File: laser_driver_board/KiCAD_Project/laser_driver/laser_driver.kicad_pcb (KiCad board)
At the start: 2 copper layers, 76.2 x 33 mm, 10 parts, among them J1 Input, J2 Output, U1 MLD203CLNE

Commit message: Finalize laser driver board.
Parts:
- moved TP2 27.0 mm to (161.8, 105.4)
- moved TP1 17.9 mm to (154.2, 105.4)
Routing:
- net /ISENS-: track 6.46 -> 27.3 mm
- net /ISENS+: track 7.51 -> 18.5 mm
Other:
- board text added: "LG 3-0000046"
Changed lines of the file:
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@@
   (general
     (thickness 1.6)
-    (drawings 72)
-    (tracks 24)
+    (drawings 73)
+    (tracks 27)
     (zones 0)
     (modules 10)
@@
   (title_block
     (title "OFMI Laser Driver Board")
-    (date 2020-09-09)
+    (date 2020-09-11)
     (rev 4.1)
     (company "Leeman Geophysical LLC")
@@
   )
   (layers
-    (0 F.Cu signal)
+    (0 F.Cu signal hide)
     (31 B.Cu signal hide)
     (32 B.Adhes user)
@@
     (47 F.CrtYd user)
     (48 B.Fab user)
-    (49 F.Fab user)
+    (49 F.Fab user hide)
   )
   (setup
@@
   )
   (module lib_fp:5006_TestPoint (layer F.Cu)
-    (at 141.5034 92.7227)
-    (fp_text reference TP1 (at 0.0127 2.6797) (layer F.SilkS)
+    (at 154.178 105.41)
+    (fp_text reference TP1 (at -2.794 0) (layer F.SilkS)
       (effects (font (size 0.762 0.762) (thickness 0.15)))
     )
@@
   )
   (module lib_fp:5006_TestPoint (layer F.Cu)
-    (at 141.5034 87.6427)
-    (fp_text reference TP2 (at 0 -2.54) (layer F.SilkS)
+    (at 161.798 105.41)
+    (fp_text reference TP2 (at 2.921 0) (layer F.SilkS)
       (effects (font (size 0.762 0.762) (thickness 0.15)))
     )
@@
   (module lib_fp:MLD203CLN (layer F.Cu)
     (at 164.973 92.71 180)
-    (fp_text reference U1 (at 0 -10.668) (layer F.SilkS)
+    (fp_text reference U1 (at 0 10.414) (layer F.SilkS)
       (effects (font (size 1 1) (thickness 0.15)))
     )
@@
       (net 4 /LDA))
   )
-  (gr_text ISENS+ (at 144.145 92.71 90) (layer F.SilkS)
+  (gr_text "LG 3-0000046" (at 197.358 108.331) (layer B.SilkS)
+    (effects (font (size 1 1) (thickness 0.15)) (justify mirror))
+  )
+  (gr_text ISENS+ (at 154.432 107.95) (layer F.SilkS)
     (effects (font (size 0.762 0.762) (thickness 0.1905)))
   )
-  (gr_text ISENS- (at 144.145 87.63 90) (layer F.SilkS)
+  (gr_text ISENS- (at 162.052 107.95) (layer F.SilkS)
     (effects (font (size 0.762 0.762) (thickness 0.1905)))
   )
@@
   (segment (start 177.4317 90.17) (end 181.991 90.17) (width 1.27) (layer F.Cu) (net 6) (status 20))
   (segment (start 173.6598 86.3981) (end 177.4317 90.17) (width 1.27) (layer F.Cu) (net 6))
-  (segment (start 144.0561 90.17) (end 141.5034 92.7227) (width 1.27) (layer B.Cu) (net 7) (status 20))
-  (segment (start 147.955 90.17) (end 144.0561 90.17) (width 1.27) (layer B.Cu) (net 7) (status 10))
-  (segment (start 147.9423 87.6427) (end 147.955 87.63) (width 1.27) (layer B.Cu) (net 8) (status 30))
-  (segment (start 141.5034 87.6427) (end 147.9423 87.6427) (width 1.27) (layer B.Cu) (net 8) (status 30))
+  (segment (start 154.178 103.571523) (end 154.178 105.41) (width 1.27) (layer B.Cu) (net 7))
+  (segment (start 154.178 95.190919) (end 154.178 103.571523) (width 1.27) (layer B.Cu) (net 7))
+  (segment (start 149.157081 90.17) (end 154.178 95.190919) (width 1.27) (layer B.Cu) (net 7))
+  (segment (start 147.955 90.17) (end 149.157081 90.17) (width 1.27) (layer B.Cu) (net 7))
+  (segment (start 161.798 94.996) (end 161.798 105.41) (width 1.27) (layer B.Cu) (net 8))
+  (segment (start 147.955 87.63) (end 154.432 87.63) (width 1.27) (layer B.Cu) (net 8))
+  (segment (start 154.432 87.63) (end 161.798 94.996) (width 1.27) (layer B.Cu) (net 8))
   (zone (net 1) (net_name GND) (layer F.Cu) (hatch edge 0.508)
     (connect_pads (clearance 0.508))

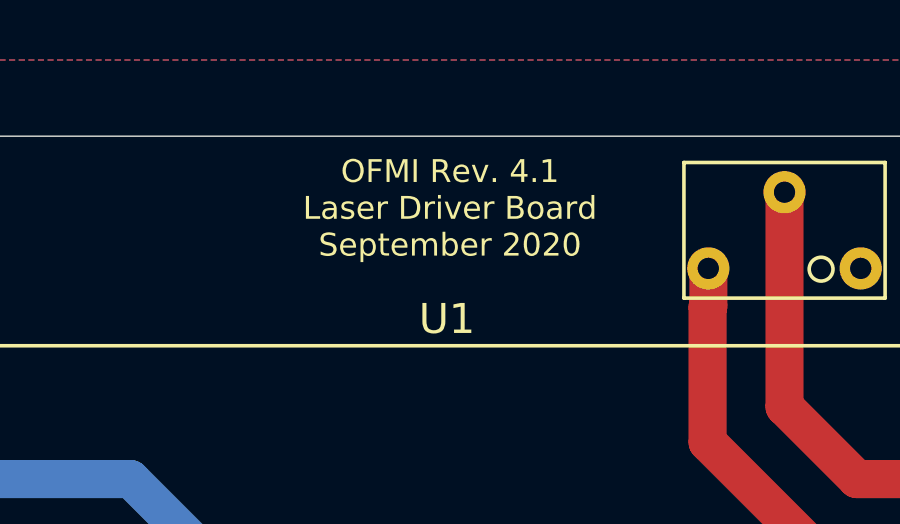
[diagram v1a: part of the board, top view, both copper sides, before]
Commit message: Rev 4.2 of laser driver board. Closes #34
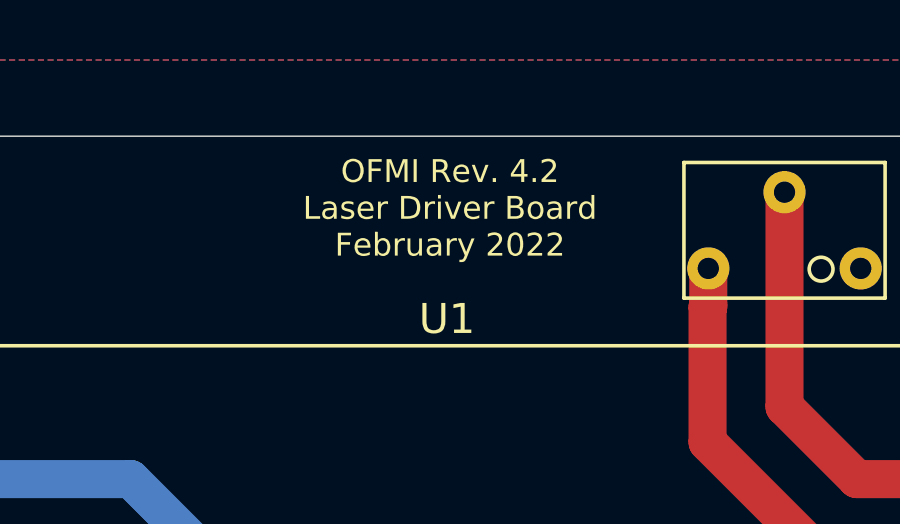
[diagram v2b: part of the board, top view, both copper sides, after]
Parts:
- added PCB1: barepcb, misc:barepcb, F.Cu at (199.9, 111.7)
- RV1: value R_POT -> 100k
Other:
- rule pad_to_mask_clearance: 0.051 -> 0
- board text added: "3-0000123"
- board text added: "OFMI Rev. 4.2 Laser Driver Board February 2022"
- board text removed: "LG 3-0000046"
- board text removed: "OFMI Rev. 4.1 Laser Driver Board September 2020"
